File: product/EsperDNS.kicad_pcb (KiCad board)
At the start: 2 copper layers, 45.1 x 83.7 mm, 57 parts, among them J1 10118192-0001LF, J2 ARJM11A3, J3 Conn_02x05_Odd_Even, Q1 Q_NMOS_GSD, Q2 Q_NMOS_GSD, Q3 Q_NMOS_GSD, SW1 SW_SPST, SW2 SW_SPST, U1 AZ1117-3.3, U2 LAN8720A, U3 ESP32-WROOM-32D

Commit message: Finished layout
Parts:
- removed C12: 0.1uF, Capacitor_SMD:C_0603_1608Metric
- removed C13: 10uF, Capacitor_SMD:C_0603_1608Metric
- removed C14, C16, C17: 1uF, Capacitor_SMD:C_0603_1608Metric
- removed D3: YLW, Diode_SMD:D_0603_1608Metric
- removed D4: RED, Diode_SMD:D_0603_1608Metric
- removed D5: BLUE, Diode_SMD:D_0603_1608Metric
- removed R0: 0, Resistor_SMD:R_0603_1608Metric
- removed R27: 100, Resistor_SMD:R_0603_1608Metric
- removed SW2: SW_SPST, Button_Switch_SMD:SW_Push_1P1T_NO_6x6mm_H9.5mm
- added C5: 0.1uF, Capacitor_SMD:C_0402_1005Metric, F.Cu at (15.7, -5.85)
- added C7: 0.1uF, Capacitor_SMD:C_0402_1005Metric, F.Cu at (13.6, -11.2)
- added FB2: Ferrite_Bead, Inductor_SMD:L_0603_1608Metric, F.Cu at (-1.00, 10.9)
- added H1: MountingHole, MountingHole:MountingHole_2.2mm_M2_Pad, F.Cu at (-20.6, 19.1)
- added H2: MountingHole, MountingHole:MountingHole_2.2mm_M2_Pad, F.Cu at (20.6, -19.1)
- C1: value 10uF -> 1uF; footprint Capacitor_SMD:C_0603_1608Metric -> Capacitor_SMD:C_0402_1005Metric
- C10: value 0.1uF -> 10uF
- C11, C2, C8: footprint Capacitor_SMD:C_0603_1608Metric -> Capacitor_SMD:C_0402_1005Metric
- C3: value 1uF -> 10uF
- C4: value 4.7uF -> 1uF; footprint Capacitor_SMD:C_0603_1608Metric -> Capacitor_SMD:C_0402_1005Metric
- C6: value 4.7uF -> 0.1uF; footprint Capacitor_SMD:C_0603_1608Metric -> Capacitor_SMD:C_0402_1005Metric
- C9: value 0.1uF -> 1uF; footprint Capacitor_SMD:C_0603_1608Metric -> Capacitor_SMD:C_0402_1005Metric
- D2: value GRN -> RS-3535MWAP; footprint Diode_SMD:D_0603_1608Metric -> LED_SMD:LED_RGB_PLCC-6
- J1: footprint digikey-footprints:USB_Micro_B_Female_10118192 -> Esper_Footprints:AMPHENOL_10118192-0001LF
- J2: value ARJM11A3 -> Conn_02x05_Odd_Even; footprint My Footprints:ARJM11A3-009-AB-ER2-T -> Esper_Footprints:CNC_3220-10-0100-00
- J3: value Conn_02x05_Odd_Even -> RJ45_Amphenol_RJMG1BD3B8K1ANR; footprint Connector_PinSocket_2.54mm:PinSocket_2x05_P2.54mm_Vertical -> Connector_RJ:RJ45_Amphenol_RJMG1BD3B8K1ANR
- Q1, Q2, Q3: footprint digikey-footprints:SOT-23-3 -> Package_TO_SOT_SMD:SOT-23
- R1, R13, R24, R8: footprint Resistor_SMD:R_0603_1608Metric -> Resistor_SMD:R_0402_1005Metric
- R10, R11, R12: value 49.9 -> 10K; footprint Resistor_SMD:R_0603_1608Metric -> Resistor_SMD:R_0402_1005Metric
- R14, R15: value 270 -> 49.9; footprint Resistor_SMD:R_0603_1608Metric -> Resistor_SMD:R_0402_1005Metric
- R16, R6, R7: value 10K -> 49.9; footprint Resistor_SMD:R_0603_1608Metric -> Resistor_SMD:R_0402_1005Metric
- R17: value 100 -> 270; footprint Resistor_SMD:R_0603_1608Metric -> Resistor_SMD:R_0402_1005Metric
- R18, R19: value 100 -> 49.9; footprint Resistor_SMD:R_0603_1608Metric -> Resistor_SMD:R_0402_1005Metric
- R2: value 470 -> 10K; footprint Resistor_SMD:R_0603_1608Metric -> Resistor_SMD:R_0402_1005Metric
- R20, R22: value 470 -> 49.9; footprint Resistor_SMD:R_0603_1608Metric -> Resistor_SMD:R_0402_1005Metric
- R21: value 470 -> 270; footprint Resistor_SMD:R_0603_1608Metric -> Resistor_SMD:R_0402_1005Metric
- R23: value 10K -> 12.1K; footprint Resistor_SMD:R_0603_1608Metric -> Resistor_SMD:R_0402_1005Metric
- R3, R4: value 100 -> 47
- R5: value 10K -> 82; footprint Resistor_SMD:R_0603_1608Metric -> Resistor_SMD:R_1206_3216Metric
- R9: value 12.1K -> 49.9; footprint Resistor_SMD:R_0603_1608Metric -> Resistor_SMD:R_0402_1005Metric
- SW1: value SW_SPST -> PTS645VH83-2 LFS; footprint Button_Switch_SMD:SW_Push_1P1T_NO_6x6mm_H9.5mm -> Button_Switch_THT:SW_Tactile_SPST_Angled_PTS645Vx83-2LFS
- U1: value AZ1117-3.3 -> AZ1117EH-3.3
- U2: value LAN8720A -> ESP32-WROOM-32D; footprint Package_DFN_QFN:QFN-24-1EP_4x4mm_P0.5mm_EP2.6x2.6mm -> RF_Module:ESP32-WROOM-32
- U3: value ESP32-WROOM-32D -> LAN8720A; footprint RF_Module:ESP32-WROOM-32 -> Package_DFN_QFN:QFN-24-1EP_4x4mm_P0.5mm_EP2.6x2.6mm_ThermalVias
- moved J2 200.8 mm to (-12.3, 9.50), turned to 90 degrees
- moved R9 198.3 mm to (-3.71, -12.3), turned to 0 degrees
- moved U2 197.4 mm to (-14.7, -6.64), turned to 0 degrees
- moved D1 196.0 mm to (2.50, -20.7), turned to 270 degrees
- moved R10 192.5 mm to (7.60, -18.1), turned to 270 degrees
- moved R1 190.1 mm to (2.55, -17.7), turned to 90 degrees
- moved R8 187.0 mm to (-17.5, 9.35)
- moved R12 186.5 mm to (4.60, 0.41)
- moved R4 181.1 mm to (0.85, -2.33)
- moved J1 180.9 mm to (-9.95, 19.8)
- moved R7 180.5 mm to (-3.70, -8.50)
- moved R14 180.3 mm to (8.79, 2.40), turned to 0 degrees
- moved R6 180.2 mm to (-3.71, -6.10)
- moved C8 180.2 mm to (16.4, -10.2), turned to 90 degrees
- moved R11 179.7 mm to (5.80, 0.40)
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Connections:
- C10 pad 1: AVDD -> +3.3VA
- C11 pad 1: +3V3 -> +3.3VA
- C3 pad 1: VBUS -> +3V3
- C4 pad 1: +3V3 -> +3.3VA
- C6 pad 1: AVDD -> +3.3VA
- C8 pad 1: AVDD -> VDDCR
- C9 pad 1: AVDD -> VDDCR
- D2 pad 1: GND -> Net-(D2-Pad1)
- FB1 pad 1: AVDD -> VBUS
- FB1 pad 2: +3V3 -> Net-(FB1-Pad2)
- J1 pad 1: Net-(J1-Pad1) -> Net-(FB1-Pad2)
- J2 pad 1: /Page 1/TD+ -> MTMS
- J2 pad 2: /Page 1/TD- -> TX
- J2 pad 3: /Page 1/RD+ -> MTDI
- J2 pad 4: AVDD -> RX
- J2 pad 5: AVDD -> MTCK
- J2 pad 6: /Page 1/RD- -> EN
- J2 pad 7: Net-(J2-Pad7) -> MTDO
- J2 pad 8: GND -> IO0
- Q1 pad 1: YELLOW -> Red
- Q1 pad 3: Net-(D3-Pad1) -> Net-(Q1-Pad3)
- Q2 pad 1: RED -> Green
- Q2 pad 3: Net-(D4-Pad1) -> Net-(Q2-Pad3)
- Q3 pad 1: BLUE -> Blue
- Q3 pad 3: Net-(D5-Pad1) -> Net-(Q3-Pad3)
- R1 pad 1: VBUS -> +3V3
- R10 pad 1: AVDD -> +3.3VA
- R10 pad 2: /Page 1/TD+ -> MDIO
- R11 pad 1: AVDD -> +3.3VA
- R11 pad 2: /Page 1/TD- -> nRST
- R12 pad 1: AVDD -> +3.3VA
- R12 pad 2: /Page 1/RD+ -> nINT
- R13 pad 1: AVDD -> +3.3VA
- R13 pad 2: /Page 1/RD- -> /Ethernet/TD+
- R14 pad 1: AVDD -> +3.3VA
- R14 pad 2: Net-(J2-PadYLWA) -> /Ethernet/TD-
- R15 pad 1: Net-(J2-PadGRNC) -> +3.3VA
- R15 pad 2: GND -> /Ethernet/RD+
- R16 pad 1: EN -> +3.3VA
- R16 pad 2: +3V3 -> /Ethernet/RD-
- R17 pad 1: Net-(R17-Pad1) -> +3.3VA
- R17 pad 2: TXD0 -> /Ethernet/LEDY_A
- R18 pad 1: Net-(R18-Pad1) -> /Ethernet/RX0_R
- R18 pad 2: TXEN -> RXD0
- R19 pad 1: Net-(R19-Pad1) -> /Ethernet/RX1_R
- R19 pad 2: TXD1 -> RXD1
- R2 pad 1: +3V3 -> EN
- R2 pad 2: Net-(D2-Pad2) -> +3V3
- R20 pad 1: VBUS -> /Ethernet/CRS_DV_R
- R20 pad 2: Net-(D3-Pad2) -> CRS_DV
- R21 pad 1: VBUS -> /Ethernet/LEDG_K
- R21 pad 2: Net-(D4-Pad2) -> GND
- R22 pad 1: VBUS -> CLK50MHZ
- R22 pad 2: Net-(D5-Pad2) -> /ESP32/CLK_R
- R23 pad 1: VBUS -> /Ethernet/RBIAS
- R23 pad 2: BLOCK -> GND
- R24 pad 1: VBUS -> /Ethernet/PHYAD0
- R24 pad 2: RESTART -> GND
- R3 pad 1: /Page 1/RX0 -> Net-(D2-Pad1)
- R3 pad 2: RXD0 -> Net-(Q3-Pad3)
- R4 pad 1: /Page 1/RX1 -> Net-(D2-Pad2)
- R4 pad 2: RXD1 -> Net-(Q2-Pad3)
- R5 pad 1: AVDD -> Net-(D2-Pad3)
- R5 pad 2: MDIO -> Net-(Q1-Pad3)
- R6 pad 1: AVDD -> /ESP32/TXD0_R
- R6 pad 2: /Page 1/nRST -> TXD0
- R7 pad 1: AVDD -> /ESP32/TXEN_R
- R7 pad 2: /Page 1/nINT -> TXEN
- R8 pad 1: /Page 1/PHYAD0 -> VBUS
- R8 pad 2: GND -> Block
- R9 pad 1: /Page 1/RBIAS -> /ESP32/TXD1_R
- R9 pad 2: GND -> TXD1
- SW1 pad 2: BLOCK -> Block
- U1 pad 4: (no net) -> +3V3
- U2 pad 1: AVDD -> GND
- U2 pad 10: /Page 1/PHYAD0 -> RXD0
- U2 pad 11: /Page 1/CRS_DV -> RXD1
- U2 pad 12: MDIO -> CRS_DV
- U2 pad 13: MDC -> MTMS
- U2 pad 14: /Page 1/nINT -> MTDI
- U2 pad 15: /Page 1/nRST -> GND
- U2 pad 16: TXEN -> MTCK
- U2 pad 17: TXD0 -> Net-(U2-Pad17)
- U2 pad 18: TXD1 -> Net-(U2-Pad18)
- U2 pad 19: AVDD -> Net-(U2-Pad19)
- U2 pad 2: LED2_nINTSEL -> +3V3
- U2 pad 20: /Page 1/TD- -> Net-(U2-Pad20)
- U2 pad 21: /Page 1/TD+ -> Net-(U2-Pad21)
- U2 pad 22: /Page 1/RD- -> Net-(U2-Pad22)
- U2 pad 23: /Page 1/RD+ -> MTDO
- U2 pad 24: /Page 1/RBIAS -> Net-(U2-Pad24)
- U2 pad 25: GND -> IO0
- U2 pad 3: LED1_REGOFF -> EN
- U2 pad 5: CLK50MHZ -> Net-(U2-Pad5)
- U2 pad 6: VDDCR -> Block
- U2 pad 7: /Page 1/RX1 -> nINT
- U2 pad 8: /Page 1/RX0 -> Red
- U2 pad 9: +3V3 -> Green
- U3 pad 1: GND -> +3.3VA
- U3 pad 10: RXD0 -> /Ethernet/PHYAD0
- U3 pad 11: RXD1 -> /Ethernet/CRS_DV_R
- U3 pad 12: CRS_DV_r -> MDIO
- U3 pad 13: BLUE -> MDC
- U3 pad 14: Net-(U3-Pad14) -> nINT
- U3 pad 15: GND -> nRST
- U3 pad 16: Net-(U3-Pad16) -> TXEN
- U3 pad 17: Net-(U3-Pad17) -> TXD0
- U3 pad 18: Net-(U3-Pad18) -> TXD1
- U3 pad 19: Net-(U3-Pad19) -> +3.3VA
- U3 pad 2: +3V3 -> LED2_nINTSEL
- U3 pad 20: Net-(U3-Pad20) -> /Ethernet/TD-
- U3 pad 21: Net-(U3-Pad21) -> /Ethernet/TD+
- U3 pad 22: Net-(U3-Pad22) -> /Ethernet/RD-
- U3 pad 23: CLKEN -> /Ethernet/RD+
- U3 pad 24: Net-(U3-Pad24) -> /Ethernet/RBIAS
- U3 pad 25: BOOTMODE -> GND
- U3 pad 3: EN -> LED1_REGOFF
- U3 pad 5: Net-(U3-Pad5) -> CLK50MHZ
- U3 pad 6: RESTART -> VDDCR
- U3 pad 7: BLOCK -> /Ethernet/RX1_R
- U3 pad 8: RED -> /Ethernet/RX0_R
- U3 pad 9: YELLOW -> +3V3
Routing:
- net +3V3: track 134.1 -> 20.1 mm, vias 6 -> 12
- net AVDD: track 107.6 -> 0.00 mm, vias 4 -> 0
- net VBUS: track 116.4 -> 36.4 mm
- net CRS_DV: track 0.00 -> 49.9 mm, vias 0 -> 2
- net nINT: track 0.00 -> 45.8 mm, vias 0 -> 3
- net CRS_DV_r: track 43.1 -> 0.00 mm, vias 2 -> 0
- net EN: track 76.8 -> 42.8 mm, vias 2 -> 0
- net BOOTMODE: track 33.9 -> 0.00 mm, vias 1 -> 0
- net RED: track 32.7 -> 0.00 mm, vias 2 -> 0
- net RESTART: track 31.8 -> 0.00 mm
- net BLOCK: track 29.4 -> 0.00 mm
- net GND: track 3.67 -> 32.1 mm, vias 37 -> 49
- net +3.3VA: track 0.00 -> 27.2 mm, vias 0 -> 12
- net Blue: track 0.00 -> 27.1 mm, vias 0 -> 4
- net YELLOW: track 27.0 -> 0.00 mm, vias 2 -> 0
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- added copper zone on Pwr, net +3.3VA
- added copper zone on F.Cu, net +3V3
- added copper zone on Pwr, net +3V3
- added copper zone on B.Cu, net Earth
- added copper zone on Gnd, net GND
- removed copper zone on F.Cu, net AVDD
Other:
- board size 45.1 x 83.7 mm -> 51 x 48 mm
- copper layers 2 -> 4
- net class Default: clearance 0.1524 -> 0.127; trace_width 0.1524 -> 0.127; via_dia 0.635 -> 0.6; via_drill 0.3302 -> 0.3
- rule pad_to_mask_clearance: 0.051 -> 0
- rule trace_clearance: 0.1524 -> 0.127
- rule trace_min: 0.1524 -> 0.127
- rule via_min_drill: 0.3302 -> 0.3
- rule via_min_size: 0.635 -> 0.6
- board text removed: "3.3V"
- board text removed: "5V"
- board text removed: "BLOCK"
- board text removed: "BLU"
- board text removed: "PWR"
- board text removed: "RED"
- board text removed: "YLW"

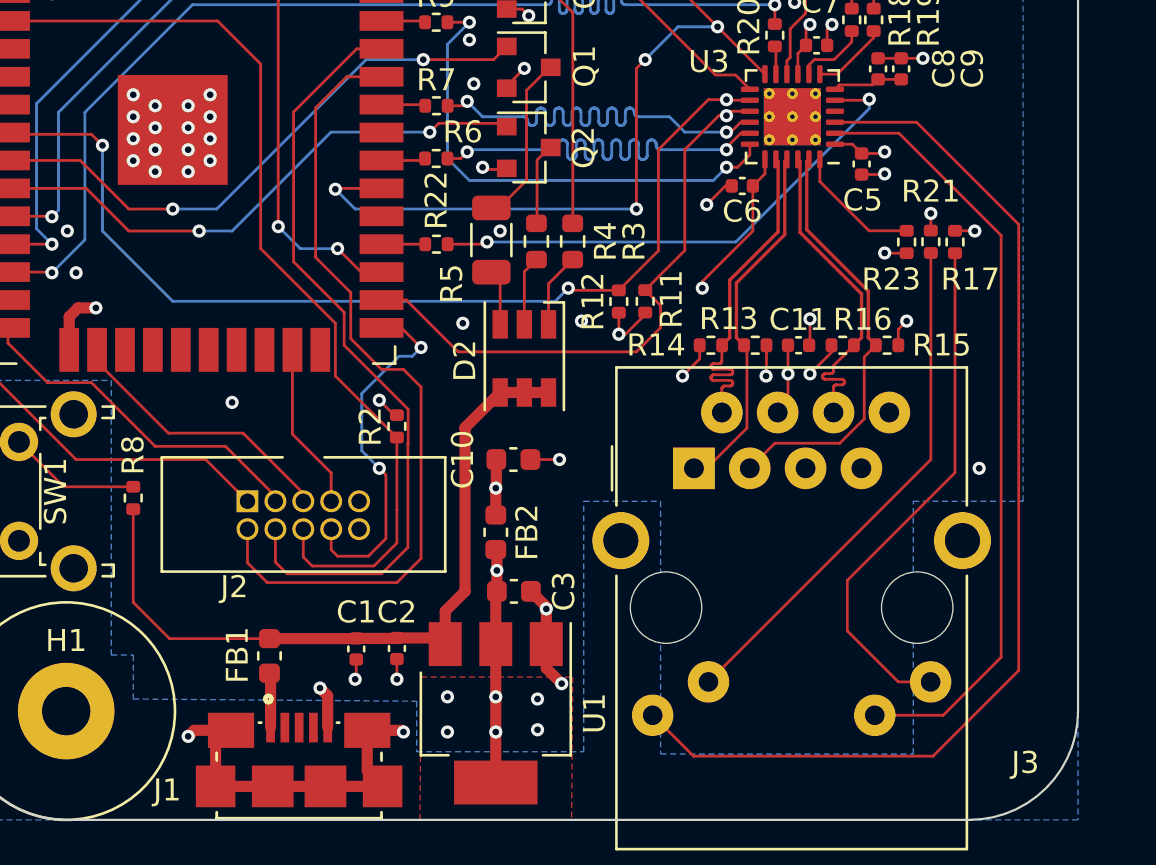
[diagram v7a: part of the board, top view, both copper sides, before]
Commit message: Added LCSC part numbers, and tweaked a few part footprints
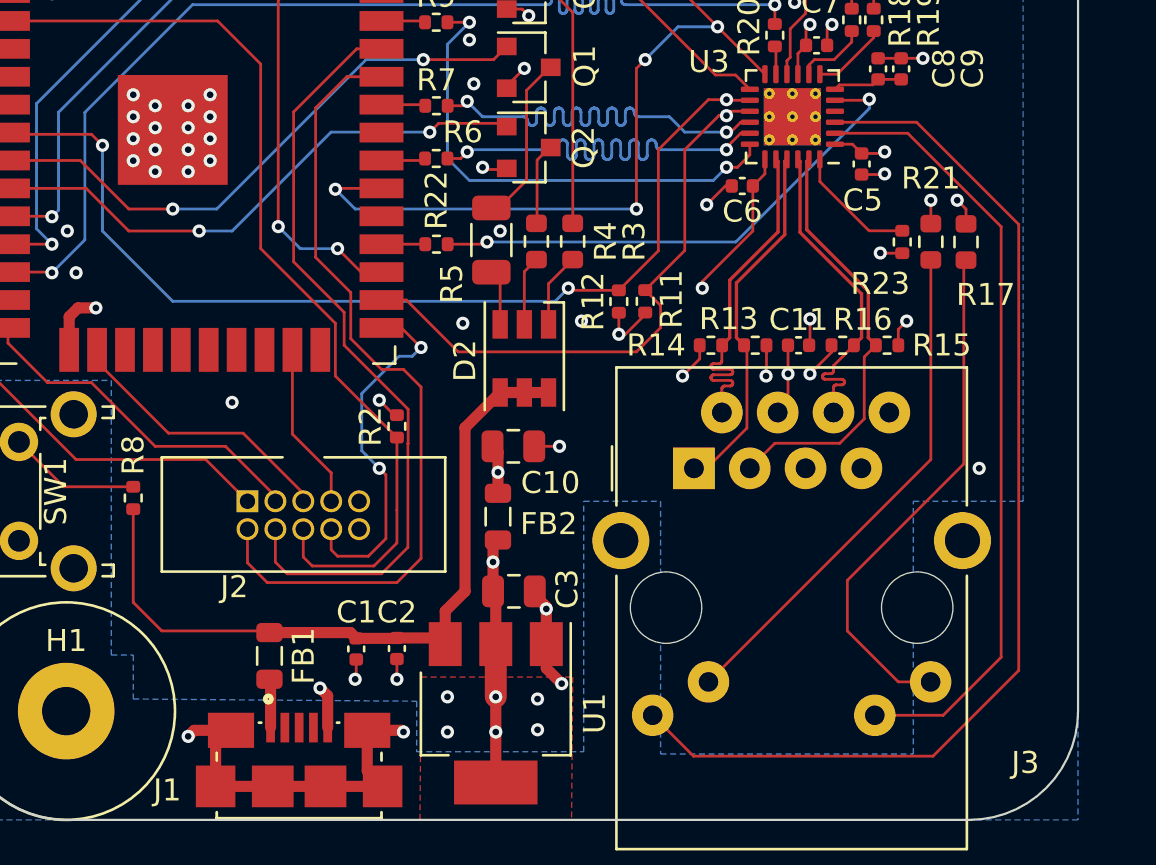
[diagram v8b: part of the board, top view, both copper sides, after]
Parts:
- C10, C3: footprint Capacitor_SMD:C_0603_1608Metric -> Capacitor_SMD:C_0805_2012Metric
- D2: value RS-3535MWAP -> RS-3535MWAR
- FB1, FB2: footprint Inductor_SMD:L_0603_1608Metric -> Inductor_SMD:L_0805_2012Metric
- Q1, Q2, Q3: value Q_NMOS_GSD -> 2N7002
- R17, R21: footprint Resistor_SMD:R_0402_1005Metric -> Resistor_SMD:R_0603_1608Metric
- U1: value AZ1117EH-3.3 -> AZ1117EH-3.3TRG1
- U2: value ESP32-WROOM-32D -> ESP32-WROOM-32E
- moved FB2 0.72 mm to (-0.90, 10.2)
- moved C10 0.60 mm to (-0.20, 7.00)
- moved R17 0.50 mm to (20.4, -2.30)
- moved R23 0.20 mm to (17.5, -2.30)
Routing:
- net GND: track 32.1 -> 32.9 mm
- net +3V3: track 20.1 -> 20.7 mm
